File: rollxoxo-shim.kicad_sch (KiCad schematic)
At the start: 70 parts, among them J1 Conn_01x10, J2 USB_C_Receptacle_USB2.0_14P, J3 Conn_01x02, J4 Conn_01x04_Pin, J5 Conn_01x01, J6 Conn_01x10, J7 Conn_01x03, J8 Conn_01x01, SW1 SW_Push, SW2 SW_Push, U1 SN74LV1T125DBV, U2 ESP32-S3FN8, U3 SN74LV1T125DBV, U4 SN74LV1T125DBV, U6 SN74LV1T125DBV, Y1 48M

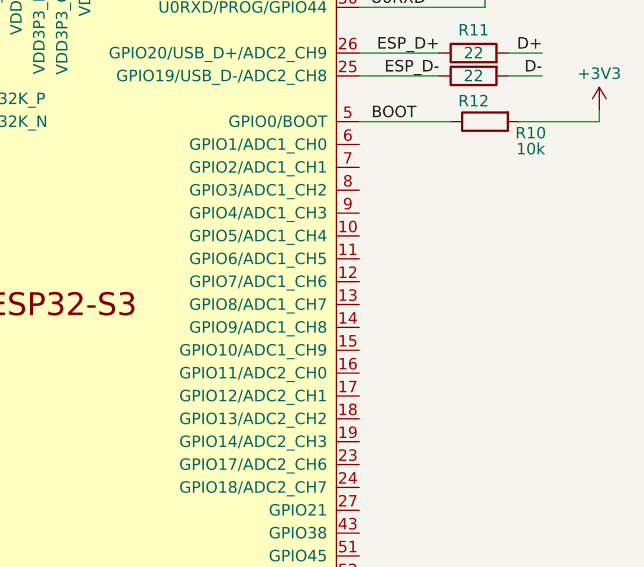
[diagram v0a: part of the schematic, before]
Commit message: schem: connect gpios
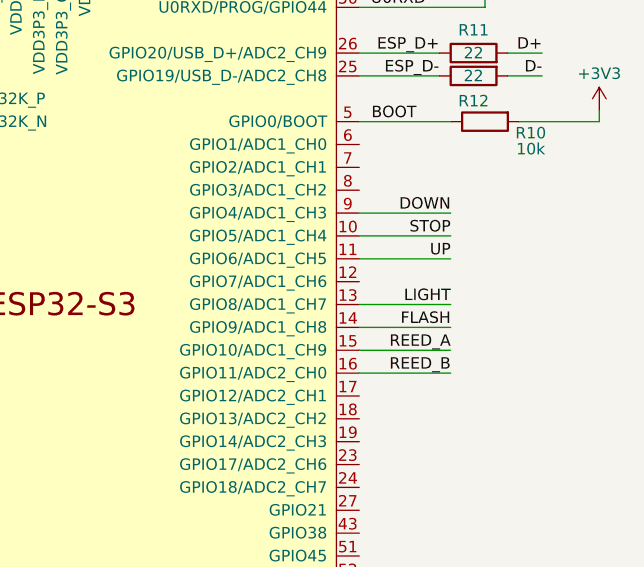
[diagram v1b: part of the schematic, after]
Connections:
- net DOWN: now also U2.9 (GPIO4/ADC1_CH3)
- net FLASH: now also U2.14 (GPIO9/ADC1_CH8)
- net LIGHT: now also U2.13 (GPIO8/ADC1_CH7)
- net REED_A: now also U2.15 (GPIO10/ADC1_CH9)
- net REED_B: now also U2.16 (GPIO11/ADC2_CH0)
- net STOP: now also U2.10 (GPIO5/ADC1_CH4)
- net UP: now also U2.11 (GPIO6/ADC1_CH5)
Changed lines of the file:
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@@
+	(wire
+		(pts
+			(xy 260.35 96.52) (xy 250.19 96.52)
+		)
+		(stroke
+			(width 0)
+			(type default)
+		)
+	)
 	(wire
 		(pts
@@
 	(wire
 		(pts
+			(xy 260.35 91.44) (xy 250.19 91.44)
+		)
+		(stroke
+			(width 0)
+			(type default)
+		)
+	)
+	(wire
+		(pts
 			(xy 250.19 68.58) (xy 264.16 68.58)
 		)
@@
 	(wire
 		(pts
+			(xy 260.35 109.22) (xy 250.19 109.22)
+		)
+		(stroke
+			(width 0)
+			(type default)
+		)
+	)
+	(wire
+		(pts
 			(xy 80.01 73.66) (xy 80.01 74.93)
 		)
@@
 	(wire
 		(pts
+			(xy 260.35 104.14) (xy 250.19 104.14)
+		)
+		(stroke
+			(width 0)
+			(type default)
+		)
+	)
+	(wire
+		(pts
 			(xy 100.33 143.51) (xy 100.33 142.24)
 		)
@@
 	(wire
 		(pts
+			(xy 260.35 106.68) (xy 250.19 106.68)
+		)
+		(stroke
+			(width 0)
+			(type default)
+		)
+	)
+	(wire
+		(pts
 			(xy 133.35 181.61) (xy 133.35 180.34)
 		)
@@
 	(wire
 		(pts
+			(xy 260.35 93.98) (xy 250.19 93.98)
+		)
+		(stroke
+			(width 0)
+			(type default)
+		)
+	)
+	(wire
+		(pts
 			(xy 100.33 100.33) (xy 86.36 100.33)
 		)
@@
 		(pts
 			(xy 177.8 30.48) (xy 191.77 30.48)
+		)
+		(stroke
+			(width 0)
+			(type default)
+		)
+	)
+	(wire
+		(pts
+			(xy 260.35 101.6) (xy 250.19 101.6)
 		)
 		(stroke
@@
 		)
 	)
+	(label "FLASH"
+		(at 260.35 104.14 180)
+		(effects
+			(font
+				(size 1.27 1.27)
+			)
+			(justify right bottom)
+		)
+	)
 	(label "XTAL_N"
 		(at 105.41 142.24 180)
@@
 		)
 	)
+	(label "REED_B"
+		(at 260.35 109.22 180)
+		(effects
+			(font
+				(size 1.27 1.27)
+			)
+			(justify right bottom)
+		)
+	)
 	(label "XTAL_P"
 		(at 76.2 142.24 0)
@@
 		)
 	)
+	(label "LIGHT"
+		(at 260.35 101.6 180)
+		(effects
+			(font
+				(size 1.27 1.27)
+			)
+			(justify right bottom)
+		)
+	)
 	(label "STOP"
 		(at 27.94 93.98 0)
@@
 		)
 	)
+	(label "DOWN"
+		(at 260.35 91.44 180)
+		(effects
+			(font
+				(size 1.27 1.27)
+			)
+			(justify right bottom)
+		)
+	)
 	(label "LIGHT"
 		(at 105.41 76.2 180)
@@
 	)
 	(label "REED_A"
+		(at 260.35 106.68 180)
+		(effects
+			(font
+				(size 1.27 1.27)
+			)
+			(justify right bottom)
+		)
+	)
+	(label "REED_A"
 		(at 125.73 115.57 0)
 		(effects
@@
 		)
 	)
+	(label "STOP"
+		(at 260.35 93.98 180)
+		(effects
+			(font
+				(size 1.27 1.27)
+			)
+			(justify right bottom)
+		)
+	)
 	(label "D-"
 		(at 66.04 175.26 180)
@@
 		)
 	)
+	(label "UP"
+		(at 260.35 96.52 180)
+		(effects
+			(font
+				(size 1.27 1.27)
+			)
+			(justify right bottom)
+		)
+	)

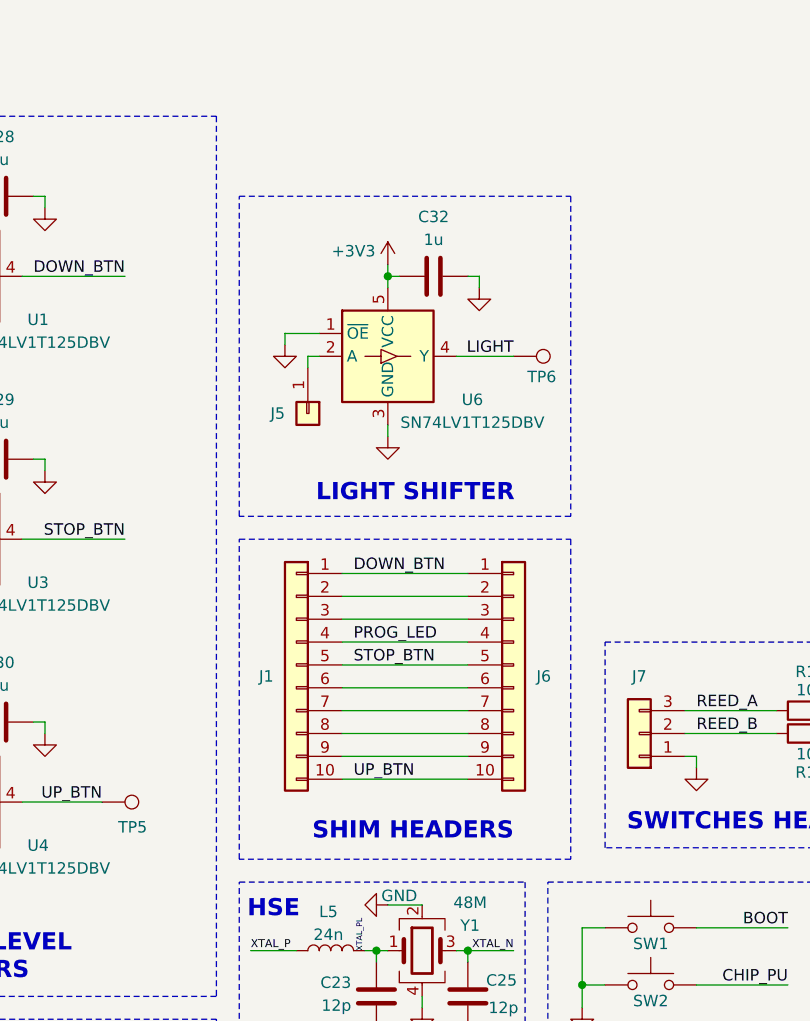
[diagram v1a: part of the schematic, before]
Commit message: schem: add +5v from shim
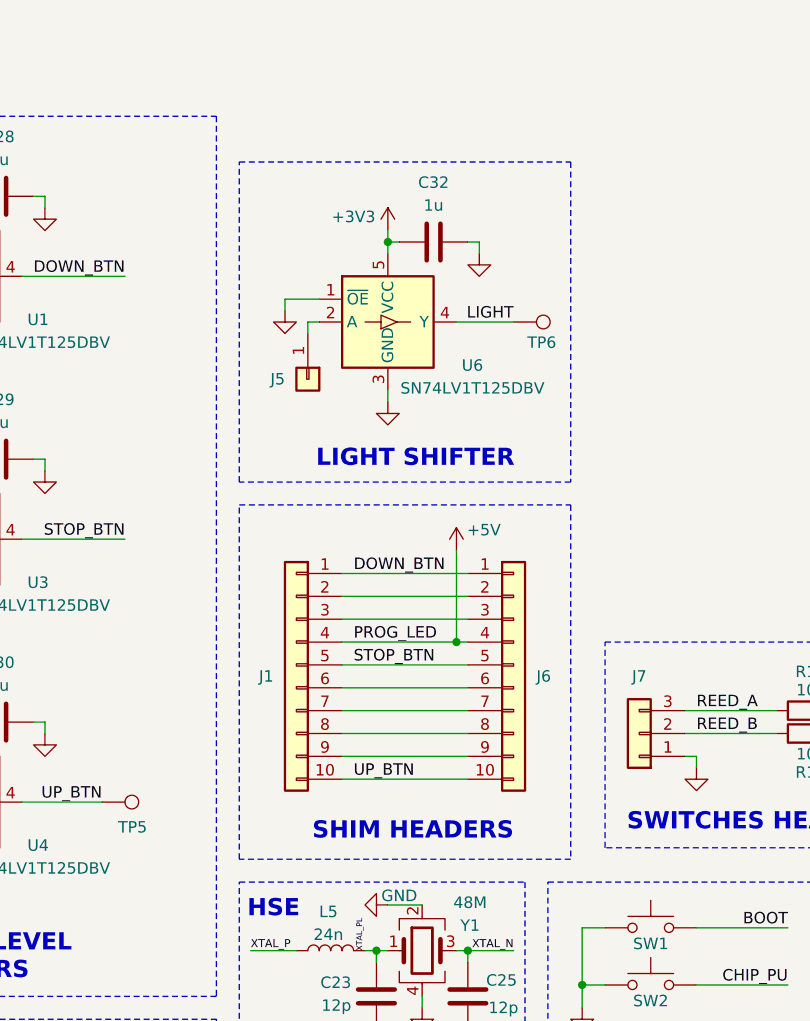
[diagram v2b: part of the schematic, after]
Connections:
- net PROG_LED is gone; now on net +5V: J1.4 (Pin_4), J6.4 (Pin_4)
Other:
- moved on the sheet: C32, J5, TP6, U6

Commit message: schem: run and fix ERC
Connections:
- no-connect marks 13 -> 37
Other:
- moved on the sheet: C32, J5, TP6, U6

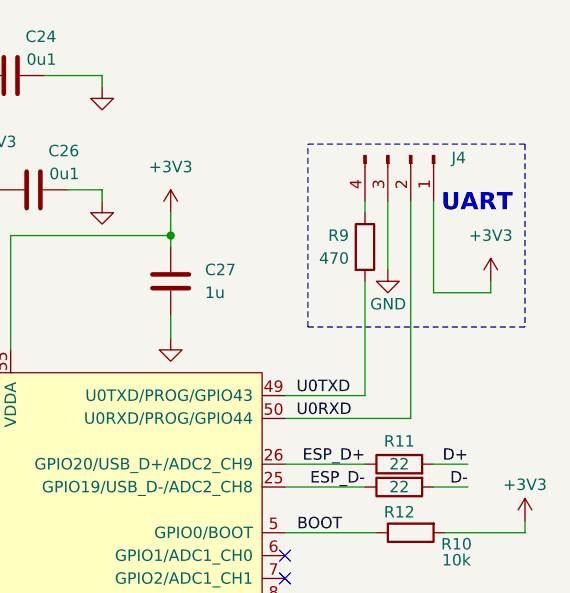
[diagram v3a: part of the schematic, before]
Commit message: schem: remove uart headers
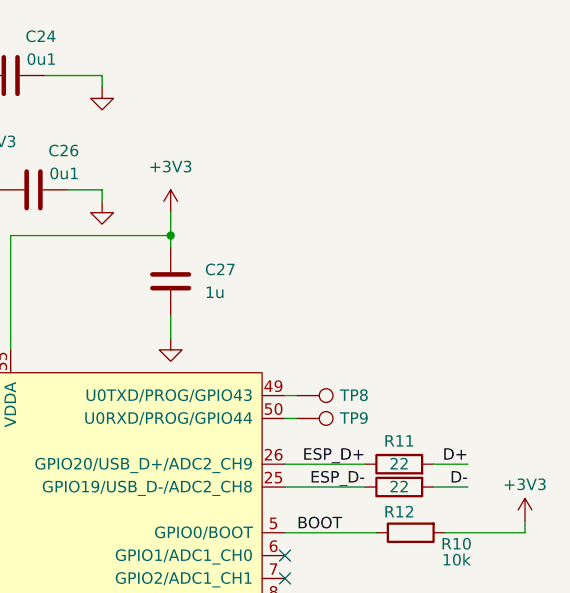
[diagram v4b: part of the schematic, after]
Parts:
- removed J4: Conn_01x04_Pin, Connector_PinHeader_2.54mm:PinHeader_1x04_P2.54mm_Vertical, symbol Connector:Conn_01x04_Pin
- removed R9: 470, Resistor_SMD:R_0402_1005Metric, symbol Device:R
- added TP8, TP9: TestPoint, TestPoint:TestPoint_Pad_D1.0mm, symbol Connector:TestPoint
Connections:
- net U0RXD: no longer names the net of U2.50 (U0RXD/PROG/GPIO44)
- net U0RXD: now also TP9.1
- net U0TXD: no longer names the net of U2.49 (U0TXD/PROG/GPIO43)
- net U0TXD: now also TP8.1
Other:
- note removed: "UART"

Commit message: schem: assign footprints
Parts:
- J7: footprint (none) -> Connector_JST:JST_XH_S3B-XH-A_1x03_P2.50mm_Horizontal
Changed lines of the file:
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@@
 			)
 		)
-		(property "Footprint" ""
+		(property "Footprint" "Connector_JST:JST_XH_S3B-XH-A_1x03_P2.50mm_Horizontal"
 			(at 119.38 118.11 0)
 			(hide yes)

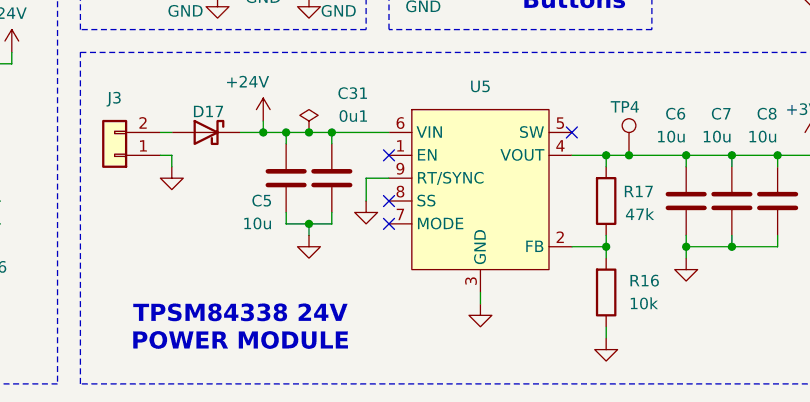
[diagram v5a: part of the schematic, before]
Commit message: schem: add ordering info to BOM
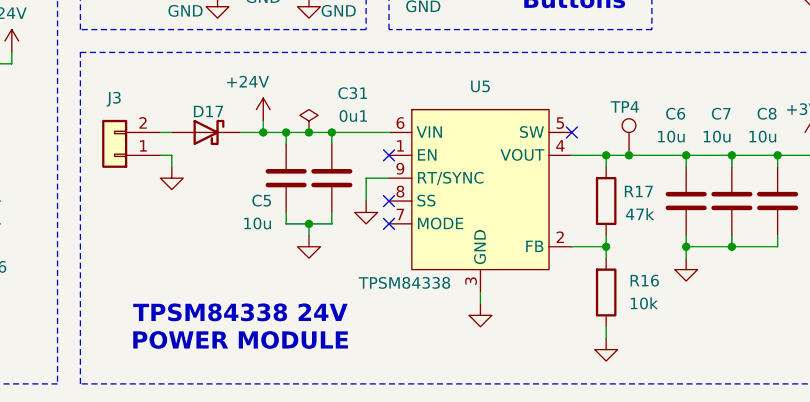
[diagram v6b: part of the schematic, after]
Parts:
- J1, J5, J6, J7, J8: now left out of the parts list
- U1, U3, U4, U6: Basic (none) -> X; JLCPCB Part # (none) -> C473338; Manufacturer (none) -> Texas Instruments; Manufacturer Part Number (none) -> SN74LV1T125DBVR
- U5: value (none) -> TPSM84338; Basic (none) -> X; JLCPCB Part # (none) -> C47122151; Manufacturer (none) -> Texas Instruments; Manufacturer Part Number (none) -> TPSM84338RCJR
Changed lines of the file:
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@@
 		(body_style 1)
 		(exclude_from_sim no)
-		(in_bom yes)
+		(in_bom no)
 		(on_board yes)
 		(in_pos_files yes)
@@
 			)
 		)
+		(property "Basic" "X"
+			(at 91.44 71.12 0)
+			(hide yes)
+			(show_name no)
+			(do_not_autoplace no)
+			(effects
+				(font
+					(size 1.27 1.27)
+				)
+			)
+		)
+		(property "JLCPCB Part #" "C473338"
+			(at 91.44 71.12 0)
+			(hide yes)
+			(show_name no)
+			(do_not_autoplace no)
+			(effects
+				(font
+					(size 1.27 1.27)
+				)
+			)
+		)
+		(property "Manufacturer" "Texas Instruments"
+			(at 91.44 71.12 0)
+			(hide yes)
+			(show_name no)
+			(do_not_autoplace no)
+			(effects
+				(font
+					(size 1.27 1.27)
+				)
+			)
+		)
+		(property "Manufacturer Part Number" "SN74LV1T125DBVR"
+			(at 91.44 71.12 0)
+			(hide yes)
+			(show_name no)
+			(do_not_autoplace no)
+			(effects
+				(font
+					(size 1.27 1.27)
+				)
+			)
+		)
 		(pin "5"
 		)
@@
 			)
 		)
+		(property "Basic" "X"
+			(at 43.18 67.31 0)
+			(hide yes)
+			(show_name no)
+			(do_not_autoplace no)
+			(effects
+				(font
+					(size 1.27 1.27)
+				)
+			)
+		)
+		(property "JLCPCB Part #" "C473338"
+			(at 43.18 67.31 0)
+			(hide yes)
+			(show_name no)
+			(do_not_autoplace no)
+			(effects
+				(font
+					(size 1.27 1.27)
+				)
+			)
+		)
+		(property "Manufacturer" "Texas Instruments"
+			(at 43.18 67.31 0)
+			(hide yes)
+			(show_name no)
+			(do_not_autoplace no)
+			(effects
+				(font
+					(size 1.27 1.27)
+				)
+			)
+		)
+		(property "Manufacturer Part Number" "SN74LV1T125DBVR"
+			(at 43.18 67.31 0)
+			(hide yes)
+			(show_name no)
+			(do_not_autoplace no)
+			(effects
+				(font
+					(size 1.27 1.27)
+				)
+			)
+		)
 		(pin "5"
 		)
@@
 		(body_style 1)
 		(exclude_from_sim no)
-		(in_bom yes)
+		(in_bom no)
 		(on_board yes)
 		(in_pos_files yes)
@@
 			)
 		)
+		(property "Basic" "X"
+			(at 43.18 125.73 0)
+			(hide yes)
+			(show_name no)
+			(do_not_autoplace no)
+			(effects
+				(font
+					(size 1.27 1.27)
+				)
+			)
+		)
+		(property "JLCPCB Part #" "C473338"
+			(at 43.18 125.73 0)
+			(hide yes)
+			(show_name no)
+			(do_not_autoplace no)
+			(effects
+				(font
+					(size 1.27 1.27)
+				)
+			)
+		)
+		(property "Manufacturer" "Texas Instruments"
+			(at 43.18 125.73 0)
+			(hide yes)
+			(show_name no)
+			(do_not_autoplace no)
+			(effects
+				(font
+					(size 1.27 1.27)
+				)
+			)
+		)
+		(property "Manufacturer Part Number" "SN74LV1T125DBVR"
+			(at 43.18 125.73 0)
+			(hide yes)
+			(show_name no)
+			(do_not_autoplace no)
+			(effects
+				(font
+					(size 1.27 1.27)
+				)
+			)
+		)
 		(pin "5"
 		)
@@
 			)
 		)
+		(property "Basic" "X"
+			(at 43.18 96.52 0)
+			(hide yes)
+			(show_name no)
+			(do_not_autoplace no)
+			(effects
+				(font
+					(size 1.27 1.27)
+				)
+			)
+		)
+		(property "JLCPCB Part #" "C473338"
+			(at 43.18 96.52 0)
+			(hide yes)
+			(show_name no)
+			(do_not_autoplace no)
+			(effects
+				(font
+					(size 1.27 1.27)
+				)
+			)
+		)
+		(property "Manufacturer" "Texas Instruments"
+			(at 43.18 96.52 0)
+			(hide yes)
+			(show_name no)
+			(do_not_autoplace no)
+			(effects
+				(font
+					(size 1.27 1.27)
+				)
+			)
+		)
+		(property "Manufacturer Part Number" "SN74LV1T125DBVR"
+			(at 43.18 96.52 0)
+			(hide yes)
+			(show_name no)
+			(do_not_autoplace no)
+			(effects
+				(font
+					(size 1.27 1.27)
+				)
+			)
+		)
 		(pin "5"
 		)
@@
 		(in_pos_files yes)
 		(dnp no)
-		(fields_autoplaced yes)
 		(property "Reference" "U5"
 			(at 119.38 162.56 0)
@@
 			)
 		)
-		(property "Value" ""
-			(at 116.84 177.8 0)
+		(property "Value" "TPSM84338"
+			(at 110.998 184.404 0)
 			(show_name no)
 			(do_not_autoplace no)
@@
 			)
 		)
+		(property "Basic" "X"
+			(at 116.84 177.8 0)
+			(hide yes)
+			(show_name no)
+			(do_not_autoplace no)
+			(effects
+				(font
+					(size 1.27 1.27)
+				)
+			)
+		)
+		(property "JLCPCB Part #" "C47122151"
+			(at 116.84 177.8 0)
+			(hide yes)
+			(show_name no)
+			(do_not_autoplace no)
+			(effects
+				(font
+					(size 1.27 1.27)
+				)
+			)
+		)
+		(property "Manufacturer" "Texas Instruments"
+			(at 116.84 177.8 0)
+			(hide yes)
+			(show_name no)
+			(do_not_autoplace no)
+			(effects
+				(font
+					(size 1.27 1.27)
+				)
+			)
+		)
+		(property "Manufacturer Part Number" "TPSM84338RCJR"
+			(at 116.84 177.8 0)
+			(hide yes)
+			(show_name no)
+			(do_not_autoplace no)
+			(effects
+				(font
+					(size 1.27 1.27)
+				)
+			)
+		)
 		(pin "9"
 		)
@@
 		(body_style 1)
 		(exclude_from_sim no)
-		(in_bom yes)
+		(in_bom no)
 		(on_board yes)
 		(in_pos_files yes)
@@
 		(body_style 1)
 		(exclude_from_sim no)
-		(in_bom yes)
+		(in_bom no)
 		(on_board yes)
 		(in_pos_files yes)
@@
 		(body_style 1)
 		(exclude_from_sim no)
-		(in_bom yes)
+		(in_bom no)
 		(on_board yes)
 		(in_pos_files yes)

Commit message: schem: add title
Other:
- company: (none) -> Rémi Ait-Younes
- title: (none) -> Rollxoxo shim
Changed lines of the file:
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@@
 	(generator_version "10.0")
 	(paper "A4")
+	(title_block
+		(title "Rollxoxo shim")
+		(date "2026-04-11")
+		(rev "01")
+		(company "Rémi Ait-Younes")
+	)
 	(rectangle
 		(start 74.93 91.44)
